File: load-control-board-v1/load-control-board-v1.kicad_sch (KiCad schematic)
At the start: 39 parts, among them CN1 3511232BMRS0BNA2, U1 LM317_SOT-223, U2 74AHC1G04, U22 TL081HIDBVR, U3 LM317_SOT-223, U5 REF5025AD, U6 SN74LVC1G123DCUR_C352969, U7 TL081HIDBVR, U8 OPA188xxDBV

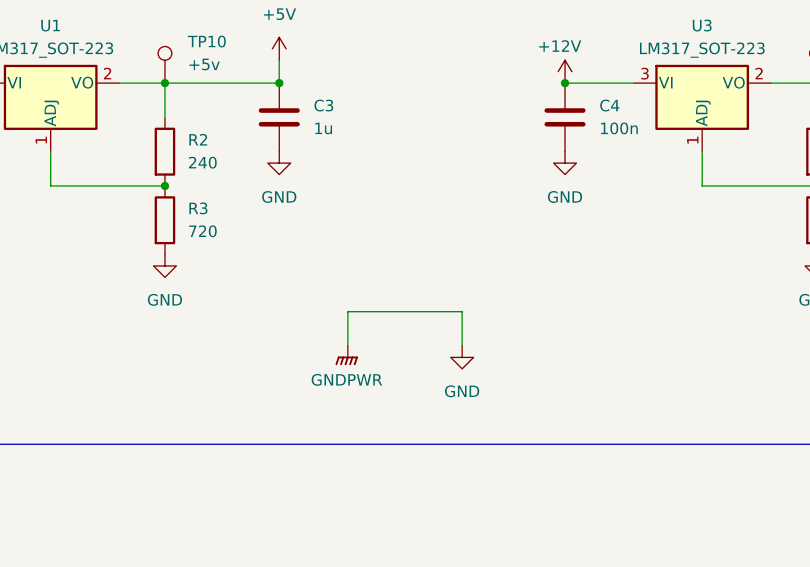
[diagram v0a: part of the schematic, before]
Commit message: Add filled zone for mosfet, change terminal to from THO to SMT
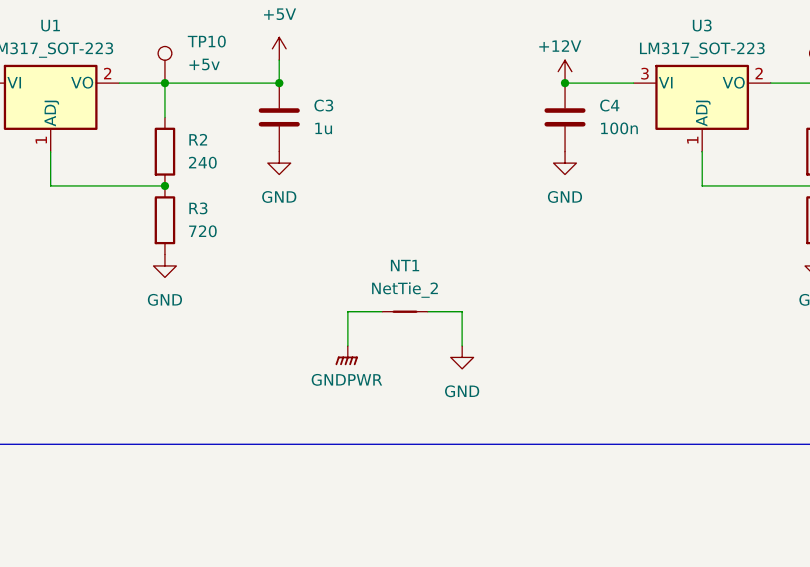
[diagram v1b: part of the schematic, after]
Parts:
- added NT1: NetTie_2, symbol Device:NetTie_2
- TP1, TP10, TP11: footprint TestPoint:TestPoint_Keystone_5015_Micro_Mini -> programmable-load-library:SMD_RH-5015
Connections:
- net GND: now also NT1.2
- new net GNDPWR: NT1.1
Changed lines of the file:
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@@
 	(wire
 		(pts
+			(xy 100.33 181.61) (xy 104.14 181.61)
+		)
+		(stroke
+			(width 0)
+			(type default)
+		)
+	)
+	(wire
+		(pts
 			(xy 212.09 93.98) (xy 212.09 88.9)
 		)
@@
 	(wire
 		(pts
+			(xy 91.44 181.61) (xy 95.25 181.61)
+		)
+		(stroke
+			(width 0)
+			(type default)
+		)
+	)
+	(wire
+		(pts
 			(xy 40.64 152.4) (xy 40.64 156.21)
 		)
@@
 	(wire
 		(pts
-			(xy 91.44 181.61) (xy 104.14 181.61)
-		)
-		(stroke
-			(width 0)
-			(type default)
-		)
-	)
-	(wire
-		(pts
 			(xy 233.68 170.18) (xy 233.68 168.91)
 		)
@@
 			)
 		)
-		(property "Footprint" "TestPoint:TestPoint_Keystone_5015_Micro_Mini"
+		(property "Footprint" "programmable-load-library:SMD_RH-5015"
 			(at 76.2 156.21 0)
 			(effects
@@
 	)
 	(symbol
+		(lib_id "Device:NetTie_2")
+		(at 97.79 181.61 0)
+		(unit 1)
+		(exclude_from_sim no)
+		(in_bom no)
+		(on_board yes)
+		(dnp no)
+		(fields_autoplaced yes)
+		(property "Reference" "NT1"
+			(at 97.79 176.53 0)
+			(effects
+				(font
+					(size 1.27 1.27)
+				)
+			)
+		)
+		(property "Value" "NetTie_2"
+			(at 97.79 179.07 0)
+			(effects
+				(font
+					(size 1.27 1.27)
+				)
+			)
+		)
+		(property "Footprint" ""
+			(at 97.79 181.61 0)
+			(effects
+				(font
+					(size 1.27 1.27)
+				)
+				(hide yes)
+			)
+		)
+		(property "Datasheet" "~"
+			(at 97.79 181.61 0)
+			(effects
+				(font
+					(size 1.27 1.27)
+				)
+				(hide yes)
+			)
+		)
+		(property "Description" "Net tie, 2 pins"
+			(at 97.79 181.61 0)
+			(effects
+				(font
+					(size 1.27 1.27)
+				)
+				(hide yes)
+			)
+		)
+		(pin "1"
+		)
+		(pin "2"
+		)
+		(instances
+			(project ""
+				(path "/932aba27-7b64-4a5e-ae3c-58efe17592af"
+					(reference "NT1")
+					(unit 1)
+				)
+			)
+		)
+	)
+	(symbol
 		(lib_name "TL081HIDBVR_1")
 		(lib_id "programmable-load-library:TL081HIDBVR")
@@
 			)
 		)
-		(property "Footprint" "TestPoint:TestPoint_Keystone_5015_Micro_Mini"
+		(property "Footprint" "programmable-load-library:SMD_RH-5015"
 			(at 45.72 152.4 0)
 			(effects
@@
 			)
 		)
-		(property "Footprint" "TestPoint:TestPoint_Keystone_5015_Micro_Mini"
+		(property "Footprint" "programmable-load-library:SMD_RH-5015"
 			(at 148.59 156.21 0)
 			(effects

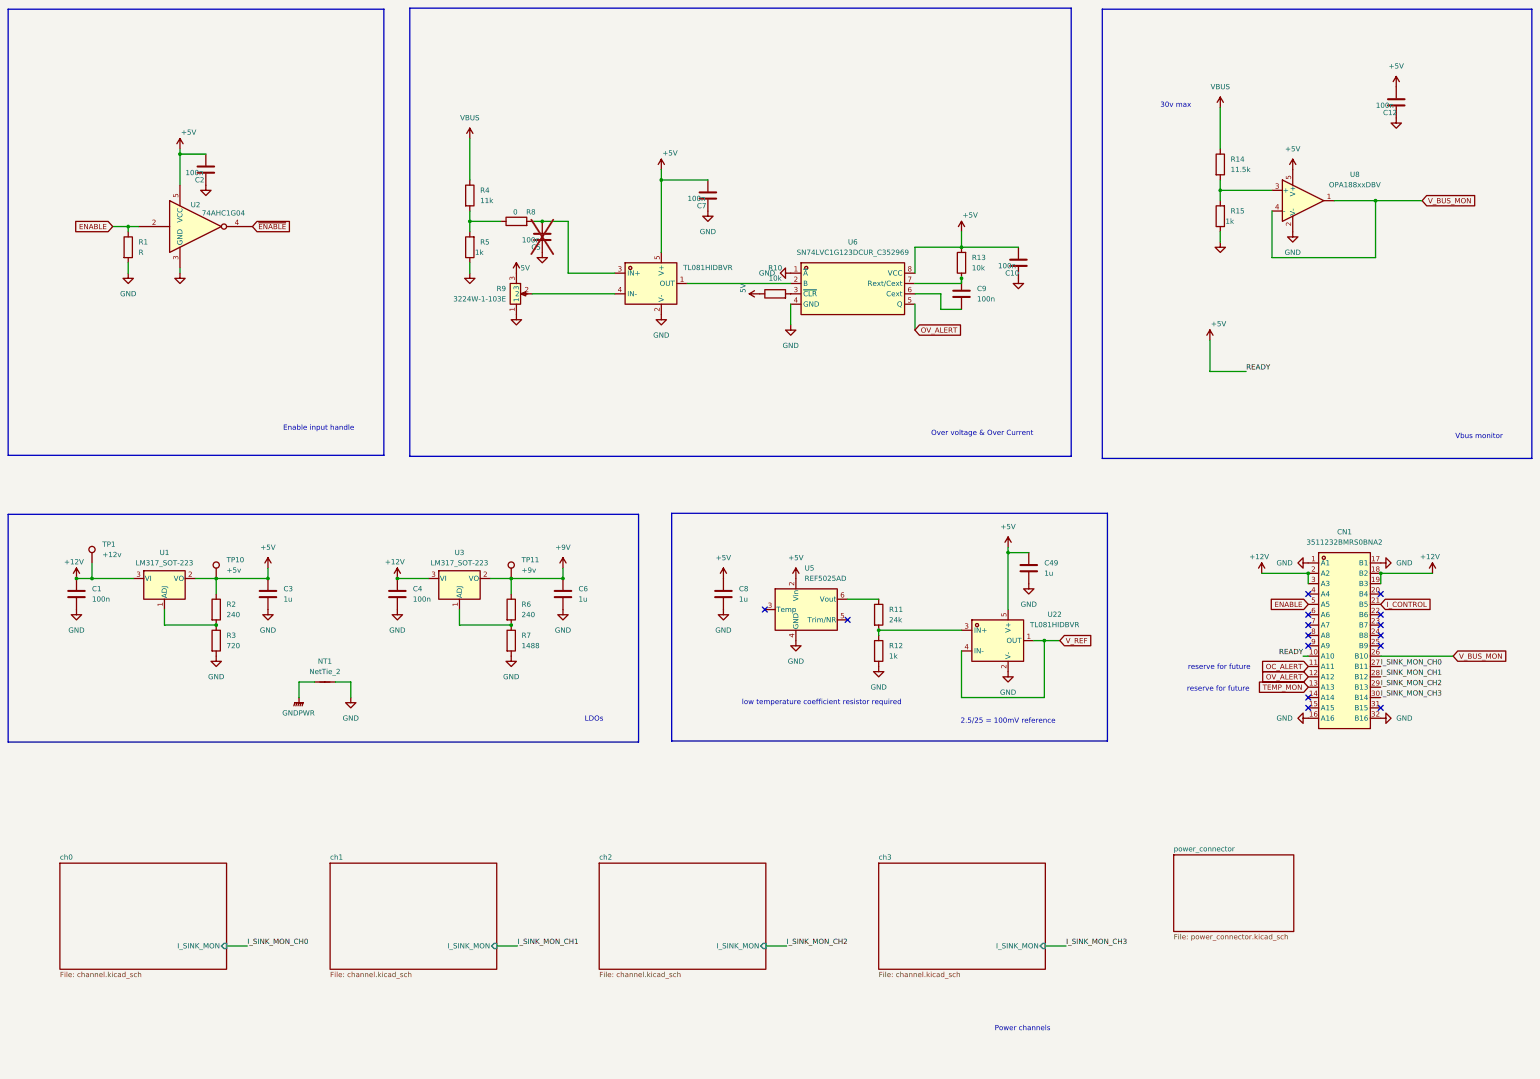
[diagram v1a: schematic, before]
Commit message: Complete second times layout (no copper filled)
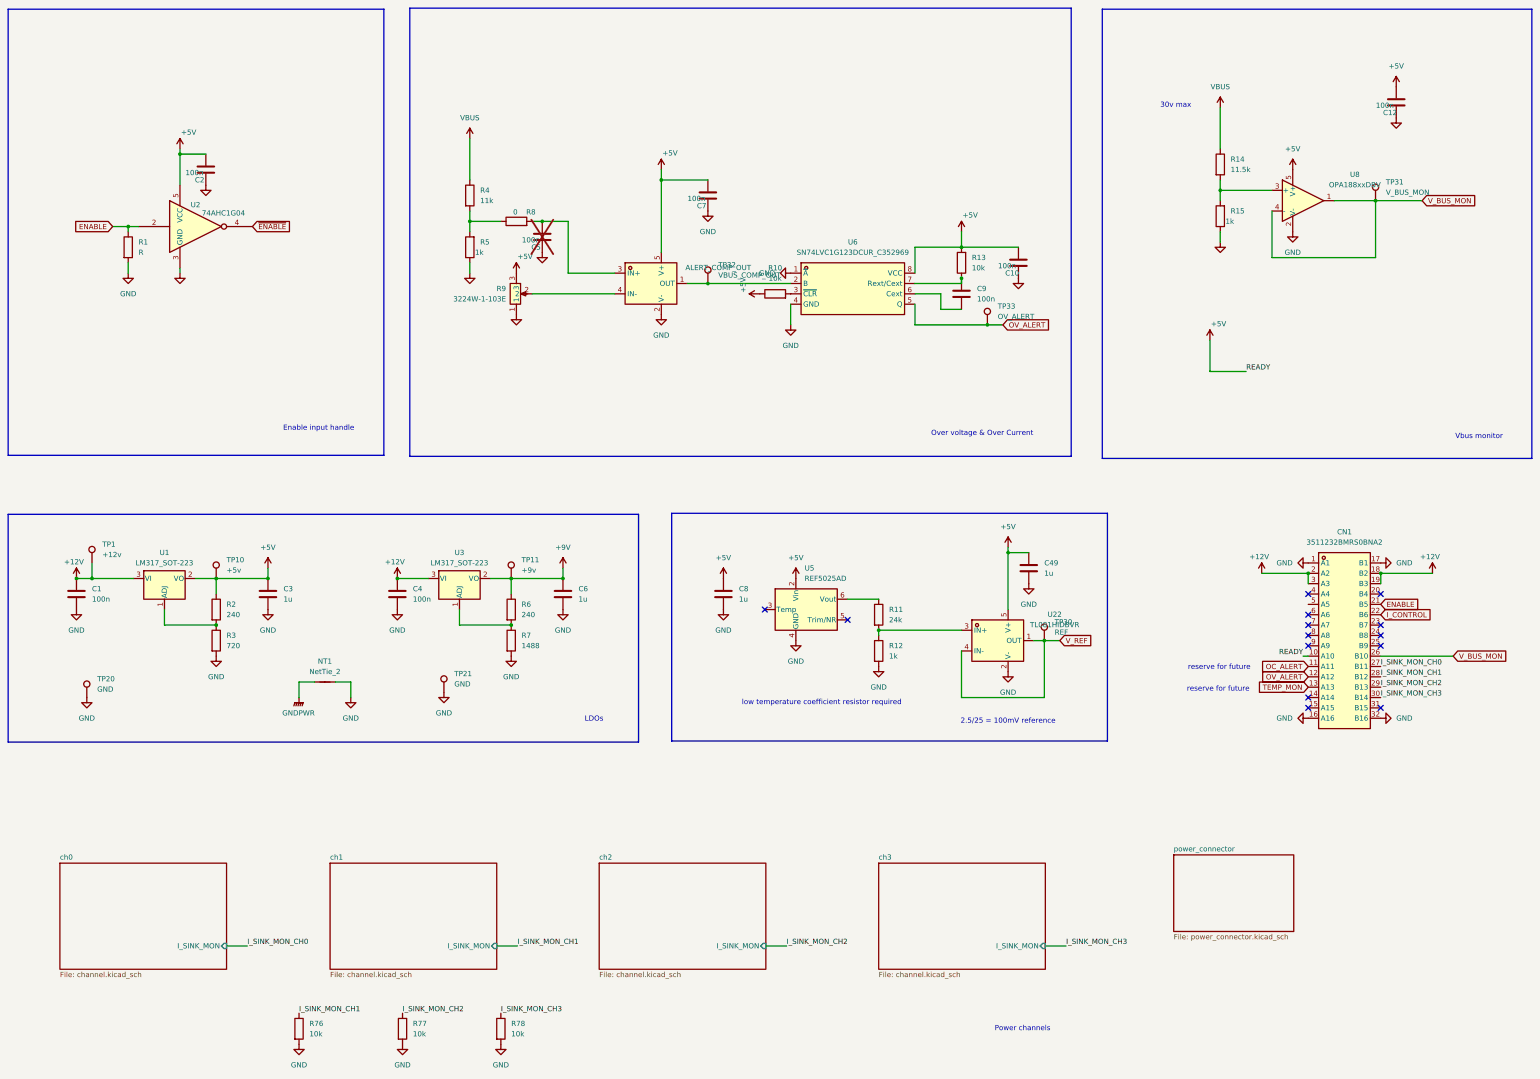
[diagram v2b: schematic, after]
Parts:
- added R76, R77, R78: 10k, Resistor_SMD:R_0603_1608Metric, symbol Device:R
- added TP20, TP21: GND, programmable-load-library:SMD_RH-5015, symbol Connector:TestPoint
- added TP30: REF, programmable-load-library:SMD_RH-5015, symbol Connector:TestPoint
- added TP31: V_BUS_MON, programmable-load-library:SMD_RH-5015, symbol Connector:TestPoint
- added TP32: VBUS_COMP_OUT, programmable-load-library:SMD_RH-5015, symbol Connector:TestPoint
- added TP33: OV_ALERT, programmable-load-library:SMD_RH-5015, symbol Connector:TestPoint
- U7: value TL081HIDBVR -> ALERT_COMP_OUT
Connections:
- net 5V is gone; now on net +5V: R10.1, R9.3
- net ENABLE: now also CN1.21 (B5); no longer CN1.5 (A5)
- net GND: now also R76.2, R77.2, R78.2, TP20.1, TP21.1
- net I_CONTROL: now also CN1.22 (B6); no longer CN1.21 (B5)
- net I_SINK_MON_CH1: now also R76.1
- net I_SINK_MON_CH2: now also R77.1
- net I_SINK_MON_CH3: now also R78.1
- net OV_ALERT: now also TP33.1
- net V_BUS_MON: now also TP31.1
- net V_REF: now also TP30.1
- net at U6.2 (B), U7.1 (OUT): now also TP32.1
- no-connect marks 15 -> 14

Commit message: First complete PCB, DRC check complete
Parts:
- NT1: footprint (none) -> NetTie:NetTie-2_SMD_Pad0.5mm
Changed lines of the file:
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@@
 			)
 		)
-		(property "Footprint" ""
+		(property "Footprint" "NetTie:NetTie-2_SMD_Pad0.5mm"
 			(at 97.79 181.61 0)
 			(effects
